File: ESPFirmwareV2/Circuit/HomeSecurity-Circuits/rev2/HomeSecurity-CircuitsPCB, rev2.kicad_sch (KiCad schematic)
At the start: 3 parts

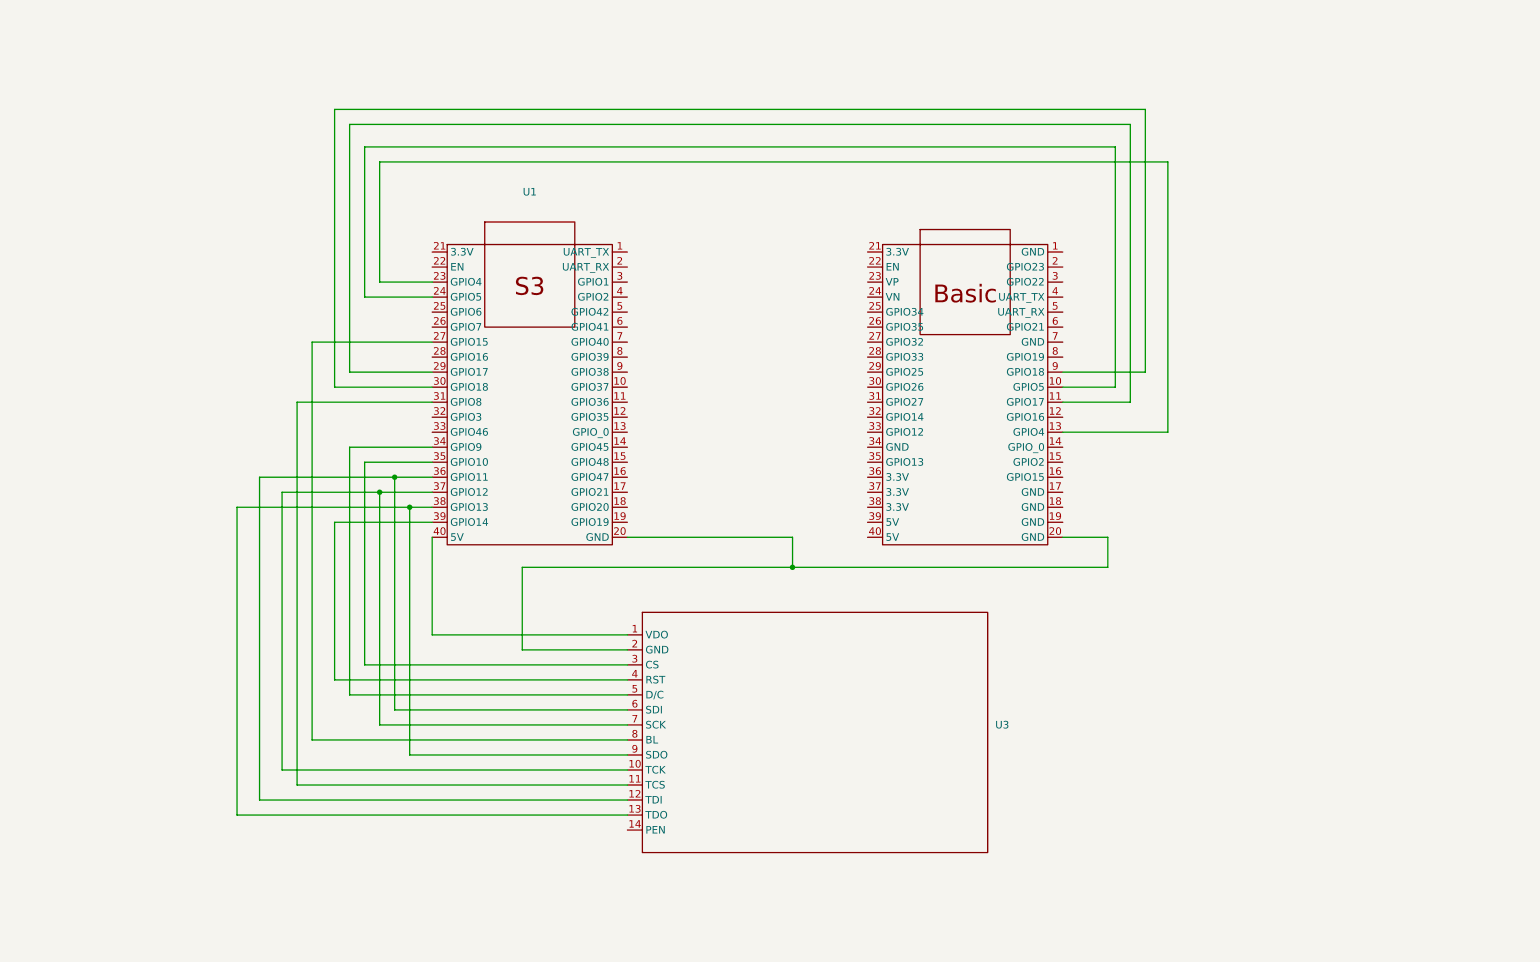
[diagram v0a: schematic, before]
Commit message: added keypad wiring
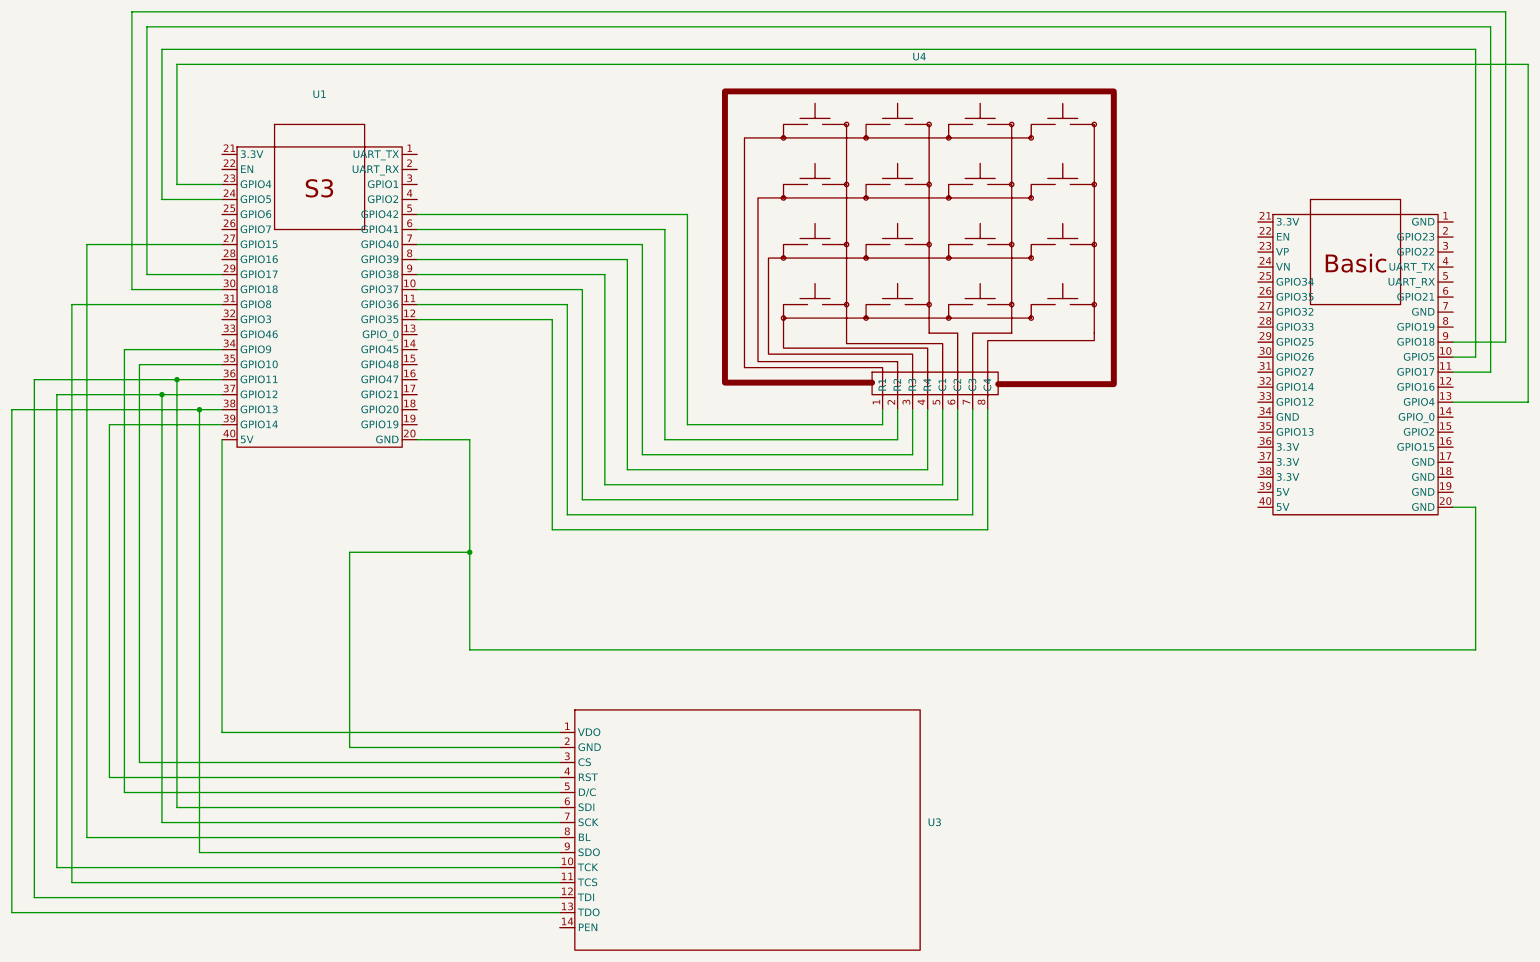
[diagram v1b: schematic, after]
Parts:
- added U4: ~, symbol HomeSecurity-Proj:keypad4x4
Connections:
- net at U1.10 (GPIO37): now also U4.6 (C2)
- net at U1.11 (GPIO36): now also U4.7 (C3)
- net at U1.12 (GPIO35): now also U4.8 (C4)
- net at U1.5 (GPIO42): now also U4.1 (R1)
- net at U1.6 (GPIO41): now also U4.2 (R2)
- net at U1.7 (GPIO40): now also U4.3 (R3)
- net at U1.8 (GPIO39): now also U4.4 (R4)
- net at U1.9 (GPIO38): now also U4.5 (C1)
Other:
- moved on the sheet: U1, U3
